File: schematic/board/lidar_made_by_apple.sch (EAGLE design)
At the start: 85 parts, among them J1 U.FL-R-SMT-1_10_, J2 U.FL-R-SMT-1_10_

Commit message: спонсор страданий
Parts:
- removed JP1, JP2: (no value), NEON-BLADE-2024:PINHD-1X8
- removed W2: (no value), NEON-BLADE-2024:VIAS-CONNECTW1.4MM
- added JP3: (no value), pinhead:PINHD-1X15
- added JP4, JP5: (no value), pinhead:PINHD-1X9
- added U$12, U$14: REF3033, NEON-BLADE-2024:REF3033
- added VR1, VR2: 3362P-1-502LF, NEON-BLADE-2024:3362P-1-502LF
- added W5: (no value), NEON-BLADE-2024:VIAS-CONNECTW1.4MM
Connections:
- removed net MISO: JP2.5, U$10.MISO
- removed net MOSI: JP2.6, U$10.MOSI
- removed net SCK: JP2.4, U$10.SCK
- removed net SSN: JP2.3, U$10.SSN
- removed net VIN: L2.2, L4.1
- new net 1MISO: JP3.3
- new net 1MOSI: JP3.2
- new net 1SCK: JP3.1
- new net 4MISO: JP5.4, U$10.MISO
- new net 4MOSI: JP5.3, U$10.MOSI
- new net 4SCK: JP5.2, U$10.SCK
- new net 5MISO: JP3.11
- new net 5MOSI: JP3.10
- new net 5SCK: JP3.9
- new net 5V: JP4.1
- new net CE_NRF: JP3.7
- new net CS_LIS: JP3.4
- new net CS_LSM: JP3.12
- new net CS_NRF: JP3.8
- new net CS_TDC: JP5.5, U$10.SSN
- new net N$28: JP3.13
- new net N$30: JP3.15
- new net N$33: R6.1, VR1.CCW
- new net N$35: R5.2, VR1.CW
- new net N$37: R22.1, VR2.CCW
- new net N$38: R23.2, VR2.CW
- new net SCL: JP4.9
- new net SDA: JP4.8
- new net SDIO_CK: JP4.5
- new net SDIO_CMD: JP4.4
- new net SDIO_DAT0: JP4.6
- new net SDIO_DAT1: JP4.7
- new net SDIO_DAT2: JP4.2
- new net SDIO_DAT3: JP4.3
- new net USIL_ON: JP5.1
- new net V_BAT: JP3.14, L2.2, L4.1, U$12.IN, U$14.IN
- net 3V3: now also JP3.5, U$12.OUT, U$14.OUT; no longer JP2.8
- net AGND: now also R26.1, U$12.GND, U$14.GND, W5.2
- net APD_FB_VOLT: now also JP5.8; no longer JP1.7
- net APD_PWM: now also JP5.9; no longer JP1.8
- net GND: now also JP3.6, W5.1; no longer JP2.7, R26.1, W2.2
- net LASER_COMP: now also JP5.6; no longer JP1.2
- net LGND: no longer W2.1
- net N$27: now also VR1.WIPER; no longer R5.2, R6.1
- net N$5: now also VR2.WIPER; no longer R22.1, R23.2
- net TDC_INT: now also JP5.7; no longer JP1.3
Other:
- moved on the sheet: C19, C23, C24, L10, R22, R23, R26, R27, R4, R6

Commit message: переделал плату лидара
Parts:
- removed R4: 10k, rcl:R-EU_R0603
- removed U$14: REF3033, NEON-BLADE-2024:REF3033
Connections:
- removed net LASER_DAC: R4.2
- removed net LGND: C16.2, C17.1, C2.1, C9.1, J2.2, R16.1, R19.1, R6.2, U$1.GND, U$1.IN-, U$11.GND, W1.1, W3.1
- removed net N$19: U$2.1S, U$2.2S
- new net 3V3_REF: C24.1, L10.1, L7.1, U$12.OUT, U$4.VCCI/VCCO
- new net PGND: C16.2, C17.1, C2.1, C6.2, C9.1, J2.2, R16.1, R19.1, R6.2, U$1.GND, U$1.IN-, U$11.GND, W1.1, W3.1
- net 3V3: no longer C24.1, L10.1, L7.1, U$12.OUT, U$14.OUT, U$4.VCCI/VCCO
- net AGND: no longer U$14.GND
- net GND: no longer C6.2
- net N$27: no longer R4.1
- net N$4: now also U$2.1S, U$2.2S
- net V_BAT: no longer U$14.IN
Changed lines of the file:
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@@
 <part name="R5" library="rcl" library_urn="urn:adsk.eagle:library:334" deviceset="R-EU_" device="R0603" package3d_urn="urn:adsk.eagle:package:23555/3" value="47k"/>
 <part name="R6" library="rcl" library_urn="urn:adsk.eagle:library:334" deviceset="R-EU_" device="R0603" package3d_urn="urn:adsk.eagle:package:23555/3" value="4.7k"/>
-<part name="R4" library="rcl" library_urn="urn:adsk.eagle:library:334" deviceset="R-EU_" device="R0603" package3d_urn="urn:adsk.eagle:package:23555/3" value="10k"/>
 <part name="L3" library="NEON-BLADE-2024" deviceset="L_10MKH" device=""/>
 <part name="L9" library="NEON-BLADE-2024" deviceset="L_BEAD" device=""/>
@@
 <part name="VR1" library="NEON-BLADE-2024" deviceset="3362P-1-502LF" device=""/>
 <part name="U$12" library="NEON-BLADE-2024" deviceset="REF3033" device=""/>
-<part name="U$14" library="NEON-BLADE-2024" deviceset="REF3033" device=""/>
 <part name="W5" library="NEON-BLADE-2024" deviceset="VIAS-CONNECT" device="W1.4MM"/>
 <part name="VR2" library="NEON-BLADE-2024" deviceset="3362P-1-502LF" device=""/>
@@
 <attribute name="VALUE" x="300.482" y="163.83" size="1.778" layer="96" rot="R90"/>
 </instance>
-<instance part="R4" gate="G$1" x="287.02" y="160.02" smashed="yes" rot="R90">
-<attribute name="NAME" x="285.5214" y="156.21" size="1.778" layer="95" rot="R90"/>
-<attribute name="VALUE" x="290.322" y="156.21" size="1.778" layer="96" rot="R90"/>
-</instance>
 <instance part="L3" gate="G$1" x="266.7" y="124.46" smashed="yes" rot="R90">
 <attribute name="NAME" x="271.78" y="123.19" size="1.778" layer="95" rot="R180"/>
@@
 </instance>
 <instance part="U$12" gate="G$1" x="50.8" y="-48.26" smashed="yes"/>
-<instance part="U$14" gate="G$1" x="271.78" y="17.78" smashed="yes"/>
 <instance part="W5" gate="G$1" x="22.86" y="-25.4" smashed="yes">
 <attribute name="NAME" x="19.05" y="-22.225" size="1.778" layer="95"/>
@@
 </busses>
 <nets>
-<net name="LGND" class="0">
+<net name="PGND" class="0">
 <segment>
 <pinref part="U$1" gate="G$1" pin="IN-"/>
@@
 <wire x1="2.54" y1="10.16" x2="2.54" y2="7.62" width="0.1524" layer="91"/>
 <label x="0.254" y="5.08" size="1.778" layer="95"/>
+</segment>
+<segment>
+<pinref part="C6" gate="G$1" pin="2"/>
+<wire x1="342.9" y1="137.16" x2="327.66" y2="137.16" width="0.1524" layer="91"/>
+<label x="327.66" y="137.16" size="1.778" layer="95"/>
 </segment>
 </net>
@@
 <net name="N$4" class="0">
 <segment>
-<pinref part="U$2" gate="G$1" pin="3S"/>
-<wire x1="60.11" y1="20.29" x2="58.42" y2="20.29" width="0.1524" layer="91"/>
-<wire x1="58.42" y1="20.29" x2="58.42" y2="12.7" width="0.1524" layer="91"/>
 <pinref part="U$3" gate="G$1" pin="C"/>
 <wire x1="58.42" y1="12.7" x2="58.42" y2="10.16" width="0.1524" layer="91"/>
 <wire x1="50.8" y1="7.62" x2="50.8" y2="12.7" width="0.1524" layer="91"/>
 <wire x1="50.8" y1="12.7" x2="58.42" y2="12.7" width="0.1524" layer="91"/>
+<pinref part="U$6" gate="G$1" pin="A"/>
+<pinref part="U$2" gate="G$1" pin="1S"/>
+<wire x1="58.42" y1="12.7" x2="58.42" y2="20.29" width="0.1524" layer="91"/>
+<wire x1="58.42" y1="20.32" x2="58.42" y2="24.29" width="0.1524" layer="91"/>
+<wire x1="58.42" y1="24.29" x2="58.42" y2="28.29" width="0.1524" layer="91"/>
+<wire x1="58.42" y1="28.29" x2="60.11" y2="28.29" width="0.1524" layer="91"/>
 <junction x="58.42" y="12.7"/>
-<pinref part="U$6" gate="G$1" pin="A"/>
+<pinref part="U$2" gate="G$1" pin="2S"/>
+<wire x1="58.42" y1="24.29" x2="60.11" y2="24.29" width="0.1524" layer="91"/>
+<pinref part="U$2" gate="G$1" pin="3S"/>
+<wire x1="58.42" y1="20.32" x2="58.42" y2="20.29" width="0.1524" layer="91"/>
+<wire x1="58.42" y1="20.29" x2="60.11" y2="20.29" width="0.1524" layer="91"/>
 </segment>
 </net>
@@
 </segment>
 <segment>
-<pinref part="C6" gate="G$1" pin="2"/>
-<wire x1="342.9" y1="137.16" x2="327.66" y2="137.16" width="0.1524" layer="91"/>
-<label x="327.66" y="137.16" size="1.778" layer="95"/>
-</segment>
-<segment>
 <pinref part="U$13" gate="G$1" pin="S"/>
 <wire x1="363.22" y1="127" x2="363.22" y2="114.3" width="0.1524" layer="91"/>
@@
 </segment>
 </net>
-<net name="N$19" class="0">
-<segment>
-<pinref part="U$2" gate="G$1" pin="2S"/>
-<wire x1="58.42" y1="20.32" x2="58.42" y2="22.86" width="0.1524" layer="91"/>
-<wire x1="58.42" y1="22.86" x2="58.42" y2="24.29" width="0.1524" layer="91"/>
-<wire x1="58.42" y1="24.29" x2="60.11" y2="24.29" width="0.1524" layer="91"/>
-<pinref part="U$2" gate="G$1" pin="1S"/>
-<wire x1="58.42" y1="24.29" x2="58.42" y2="28.29" width="0.1524" layer="91"/>
-<wire x1="58.42" y1="28.29" x2="60.11" y2="28.29" width="0.1524" layer="91"/>
-</segment>
-</net>
 <net name="TDC_CLK" class="0">
 <segment>
@@
 </segment>
 <segment>
-<wire x1="15.24" y1="-104.22" x2="15.24" y2="-116.84" width="0.1524" layer="91"/>
-<wire x1="12.7" y1="-116.84" x2="15.24" y2="-116.84" width="0.1524" layer="91"/>
-<wire x1="15.24" y1="-116.84" x2="15.24" y2="-124.46" width="0.1524" layer="91"/>
-<junction x="15.24" y="-116.84"/>
-<wire x1="15.24" y1="-124.46" x2="17.78" y2="-124.46" width="0.1524" layer="91"/>
-<pinref part="C24" gate="G$1" pin="1"/>
-<label x="12.7" y="-119.38" size="1.778" layer="95" rot="R90"/>
-<pinref part="U$4" gate="G$1" pin="VCCI/VCCO"/>
-</segment>
-<segment>
 <wire x1="124.46" y1="-25.4" x2="124.46" y2="-20.32" width="0.1524" layer="91"/>
 <label x="121.92" y="-20.32" size="1.778" layer="95"/>
@@
 </segment>
 <segment>
-<wire x1="287.02" y1="12.7" x2="287.02" y2="17.78" width="0.1524" layer="91"/>
-<label x="287.02" y="15.24" size="1.778" layer="95" rot="R90"/>
-<pinref part="L7" gate="G$1" pin="1"/>
-<pinref part="U$14" gate="G$1" pin="OUT"/>
-<wire x1="284.48" y1="17.78" x2="287.02" y2="17.78" width="0.1524" layer="91"/>
-</segment>
-<segment>
 <pinref part="JP3" gate="A" pin="5"/>
 <wire x1="195.58" y1="63.5" x2="177.8" y2="63.5" width="0.1524" layer="91"/>
 <label x="177.8" y="63.5" size="1.778" layer="95"/>
-</segment>
-<segment>
-<pinref part="U$12" gate="G$1" pin="OUT"/>
-<wire x1="66.04" y1="-48.26" x2="63.5" y2="-48.26" width="0.1524" layer="91"/>
-<pinref part="L10" gate="G$1" pin="1"/>
-<wire x1="66.04" y1="-53.34" x2="66.04" y2="-48.26" width="0.1524" layer="91"/>
-<label x="66.04" y="-48.26" size="1.778" layer="95"/>
 </segment>
 </net>
@@
 <pinref part="U$11" gate="G$1" pin="FB"/>
 <wire x1="276.86" y1="142.24" x2="287.02" y2="142.24" width="0.1524" layer="91"/>
-<pinref part="R4" gate="G$1" pin="1"/>
 <wire x1="287.02" y1="142.24" x2="287.02" y2="149.86" width="0.1524" layer="91"/>
 <pinref part="VR1" gate="G$1" pin="WIPER"/>
-<wire x1="287.02" y1="149.86" x2="287.02" y2="154.94" width="0.1524" layer="91"/>
 <wire x1="289.56" y1="149.86" x2="287.02" y2="149.86" width="0.1524" layer="91"/>
-<junction x="287.02" y="149.86"/>
-</segment>
-</net>
-<net name="LASER_DAC" class="0">
-<segment>
-<pinref part="R4" gate="G$1" pin="2"/>
-<wire x1="287.02" y1="165.1" x2="287.02" y2="172.72" width="0.1524" layer="91"/>
-<label x="279.4" y="172.72" size="1.778" layer="95"/>
 </segment>
 </net>
@@
 </segment>
 <segment>
-<pinref part="U$14" gate="G$1" pin="GND"/>
-<wire x1="271.78" y1="27.94" x2="271.78" y2="35.56" width="0.1524" layer="91"/>
-<label x="269.24" y="35.56" size="1.778" layer="95"/>
-</segment>
-<segment>
 <pinref part="W5" gate="G$1" pin="2"/>
 <wire x1="27.94" y1="-25.4" x2="27.94" y2="-27.94" width="0.1524" layer="91"/>
 <wire x1="27.94" y1="-25.4" x2="25.4" y2="-25.4" width="0.1524" layer="91"/>
 <label x="25.4" y="-30.48" size="1.778" layer="95"/>
-<wire x1="27.94" y1="-25.4" x2="30.48" y2="-25.4" width="0.1524" layer="91"/>
-<junction x="27.94" y="-25.4"/>
 </segment>
 </net>
@@
 </segment>
 <segment>
-<pinref part="U$14" gate="G$1" pin="IN"/>
-<wire x1="259.08" y1="17.78" x2="254" y2="17.78" width="0.1524" layer="91"/>
-<label x="251.46" y="17.78" size="1.778" layer="95"/>
-</segment>
-<segment>
 <label x="248.92" y="101.6" size="1.778" layer="95"/>
 <pinref part="L2" gate="G$1" pin="2"/>
@@
 </segment>
 </net>
+<net name="3V3_REF" class="0">
+<segment>
+<wire x1="287.02" y1="12.7" x2="287.02" y2="17.78" width="0.1524" layer="91"/>
+<label x="287.02" y="15.24" size="1.778" layer="95" rot="R90"/>
+<pinref part="L7" gate="G$1" pin="1"/>
+</segment>
+<segment>
+<pinref part="U$12" gate="G$1" pin="OUT"/>
+<wire x1="66.04" y1="-48.26" x2="63.5" y2="-48.26" width="0.1524" layer="91"/>
+<pinref part="L10" gate="G$1" pin="1"/>
+<wire x1="66.04" y1="-53.34" x2="66.04" y2="-48.26" width="0.1524" layer="91"/>
+<label x="66.04" y="-48.26" size="1.778" layer="95"/>
+</segment>
+<segment>
+<wire x1="15.24" y1="-104.22" x2="15.24" y2="-116.84" width="0.1524" layer="91"/>
+<wire x1="12.7" y1="-116.84" x2="15.24" y2="-116.84" width="0.1524" layer="91"/>
+<wire x1="15.24" y1="-116.84" x2="15.24" y2="-124.46" width="0.1524" layer="91"/>
+<junction x="15.24" y="-116.84"/>
+<wire x1="15.24" y1="-124.46" x2="17.78" y2="-124.46" width="0.1524" layer="91"/>
+<pinref part="C24" gate="G$1" pin="1"/>
+<label x="12.7" y="-119.38" size="1.778" layer="95" rot="R90"/>
+<pinref part="U$4" gate="G$1" pin="VCCI/VCCO"/>
+</segment>
+</net>

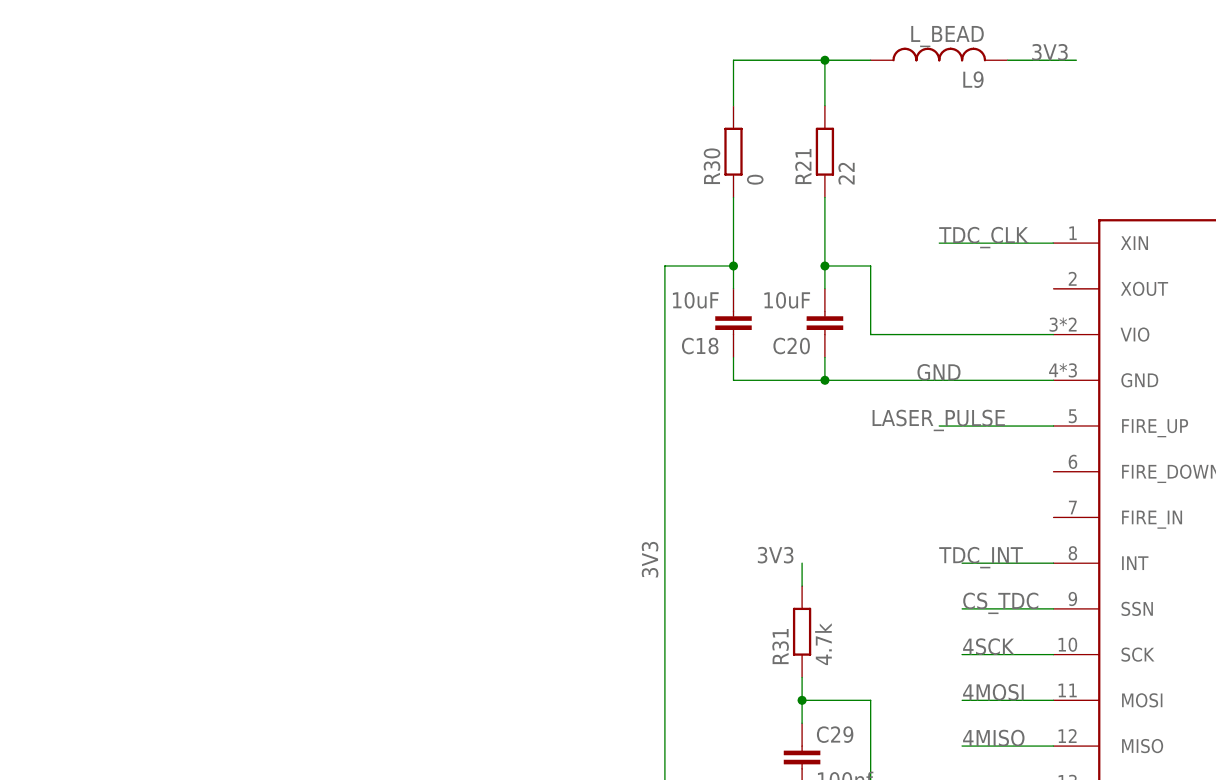
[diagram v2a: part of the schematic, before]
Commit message: немного переделал плату лидара
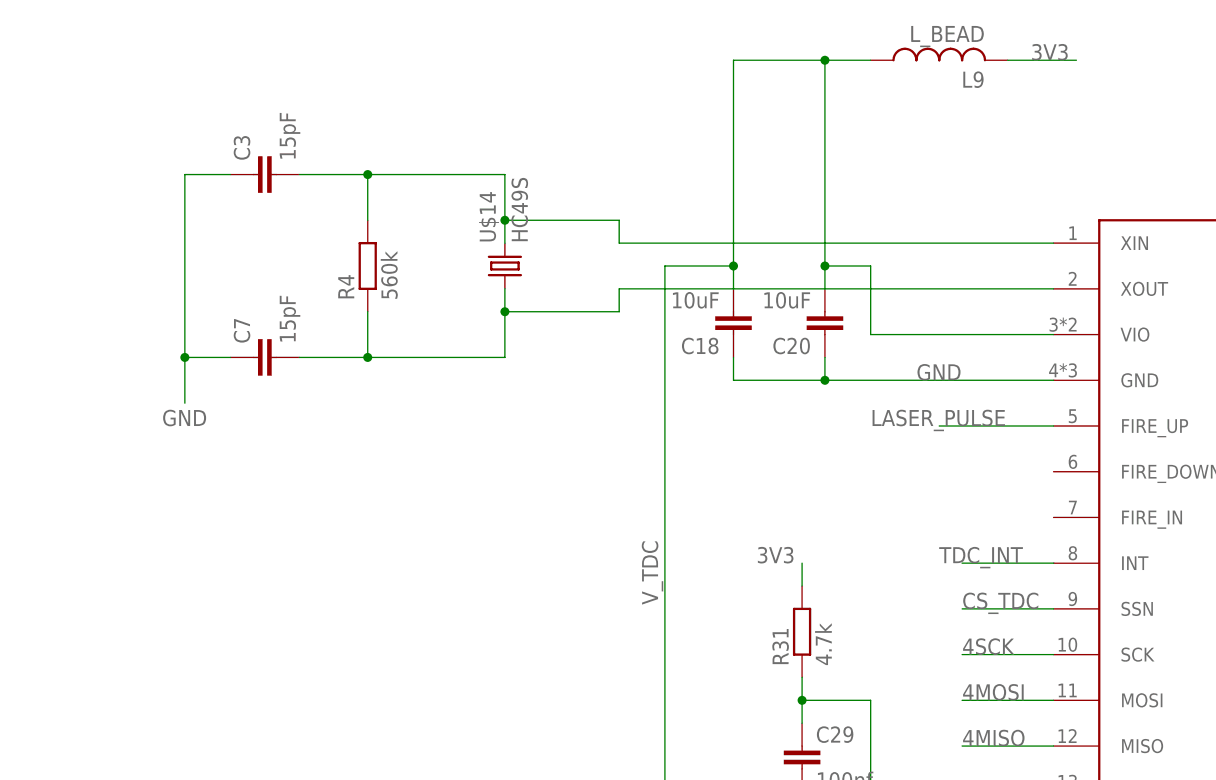
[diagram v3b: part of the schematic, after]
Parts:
- removed R21: 22, rcl:R-EU_R0603
- removed R30: 0, rcl:R-EU_R0603
- added C3, C7: 15pF, rcl:C-EUC0603
- added R4: 560k, rcl:R-EU_R0603
- added U$14: HC49S, NEON-BLADE-2024:HC49S
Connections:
- removed net N$24: L9.1, R21.2, R30.2
- removed net TDC_CLK: U$10.XIN
- new net N$19: C7.2, R4.1, U$10.XOUT, U$14.1
- new net V_TDC: C18.2, C20.2, L9.1, U$10.VCC, U$10.VIO
- net 3V3: no longer C18.2, R30.1, U$10.VCC
- net GND: now also C3.1, C7.1
- net N$23: now also C3.2, R4.2, U$10.XIN, U$14.2; no longer C20.2, R21.1, U$10.VIO
